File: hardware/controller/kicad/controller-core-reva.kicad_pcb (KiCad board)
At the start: 2 copper layers, 141.6 x 135.2 mm, 138 parts, among them J101 12V_ISOLATED_INPUT / JST XH, J102 STM_SWD / 1x6 2.54mm, J103 ESP_UART / 1x6 2.54mm, J104 UI_LINK / IDC 2x8 2.54mm, J105 JP13 NTC / 2 vías, J106 JP5 FLOW ADAPTER / VCC-GND-OC, J107 JP14 DOOR / contacto seco, J108 JP16 VISUAL V1..V8 / XH-8, J109 JP22 WATER / RED-WHITE-BLACK, J110 USB-C SERVICE / USB 2.0, J111 USB BENCH POWER / OPEN, J112 24V_ACTUATOR_INPUT / JST XH, J113 JP3 VALVE / JST XH, J114 POWER MONITOR / MEASURE ONLY, J115 JP8 GRINDER / 320VDC, J117 JP24 PUMP / 230VAC, J118 JP17 MAINS / L-N, Q501 SI2308A, U101 STM32G431RBT6, U201 ESP32-S3-WROOM-1-N8R8, U203 USBLC6-2SC6, U301 AP63203WU-7, U302 TPS22918DBVR, U501 DRV8876PWPR, U502 UCC27517DBVR, U601 TPS3828-33DBVR, U602 SN74LVC2G08DCTR

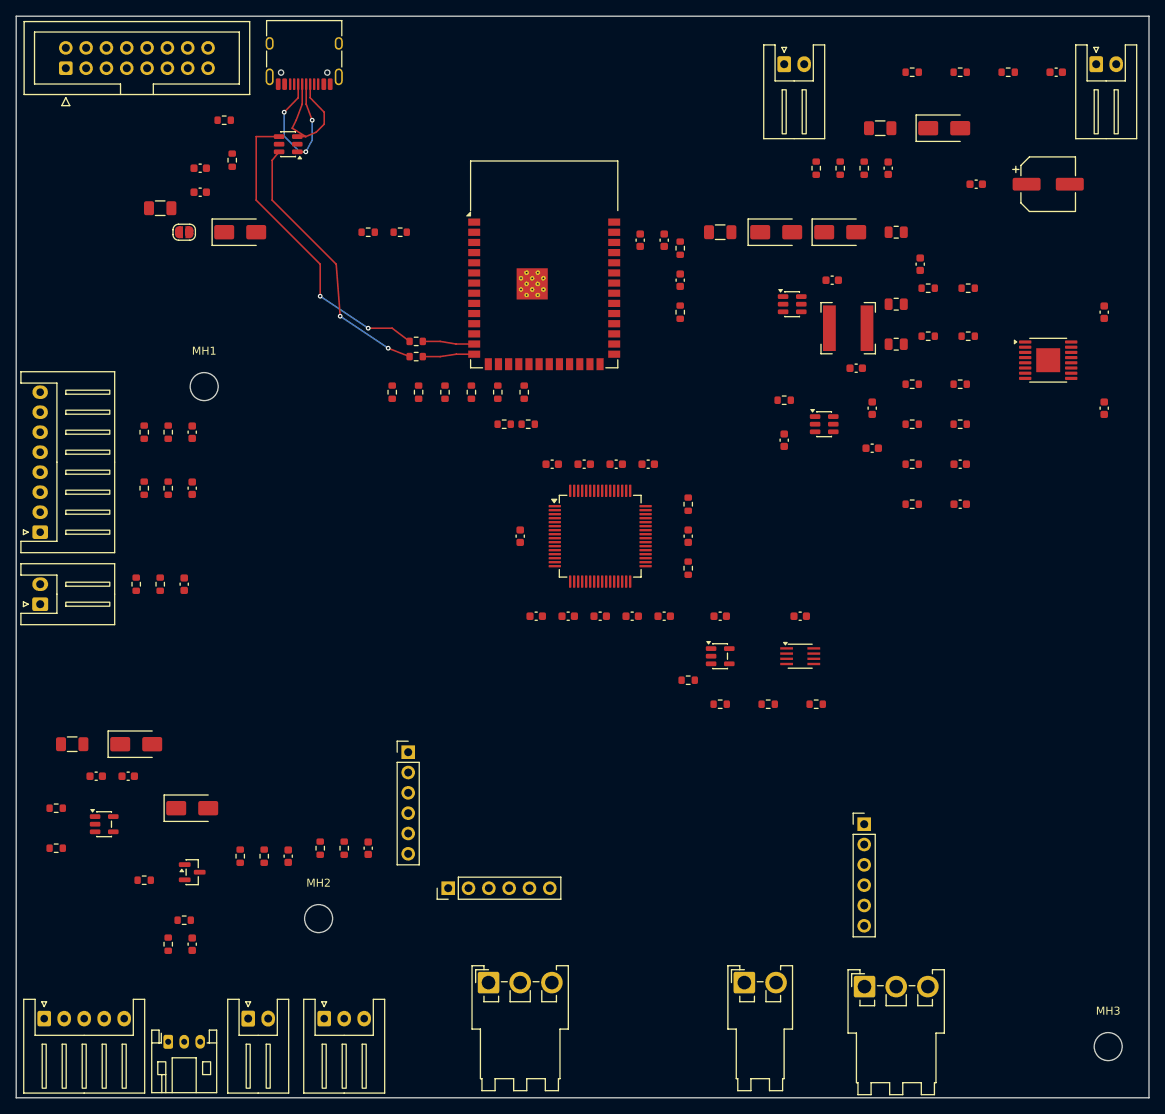
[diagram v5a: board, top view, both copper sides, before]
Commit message: Integrate onboard mains supply into controller PCB
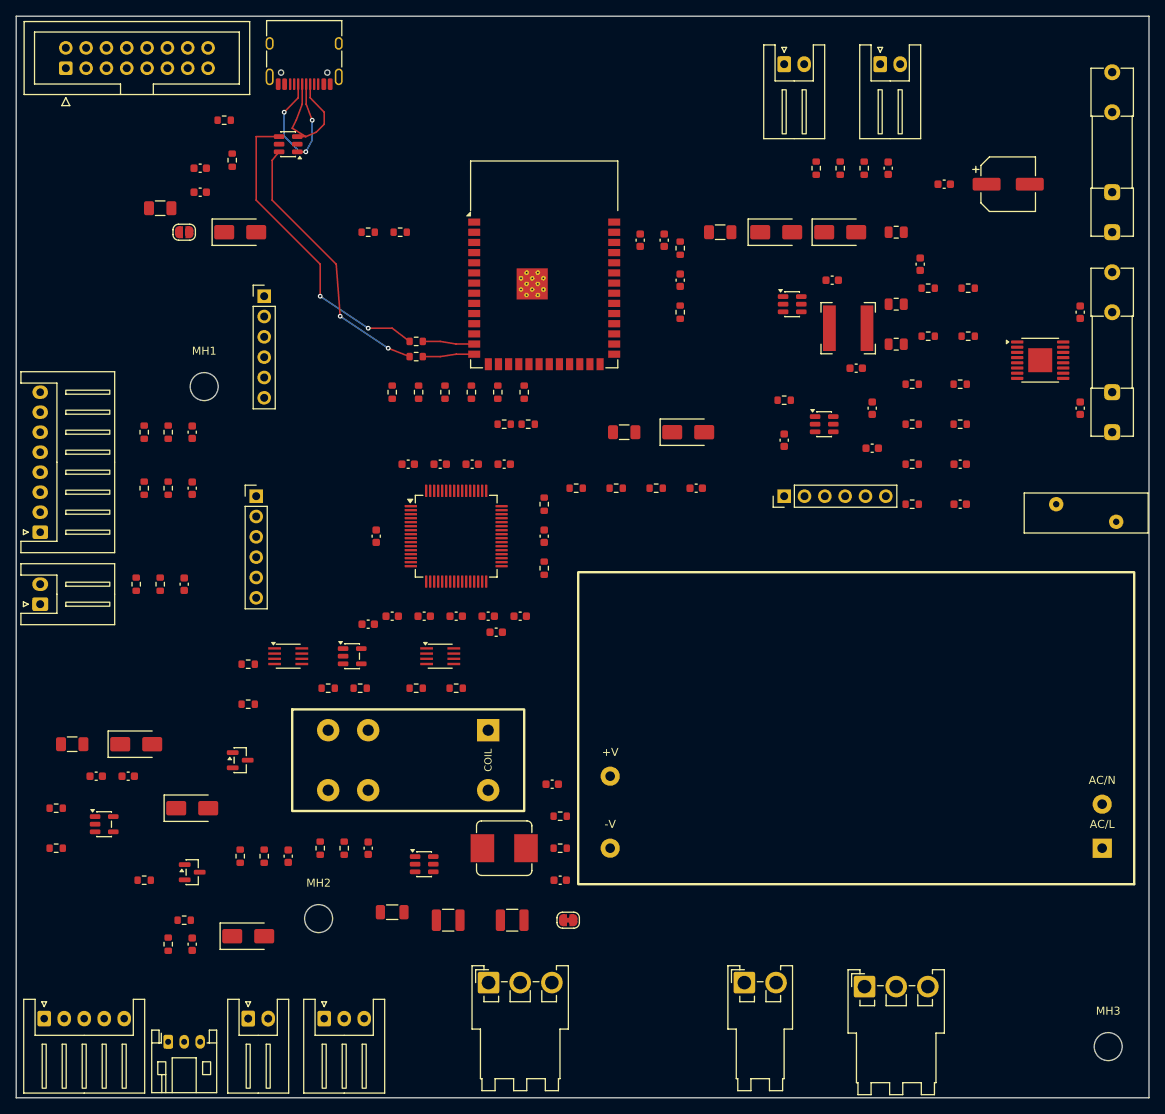
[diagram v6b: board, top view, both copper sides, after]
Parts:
- added C310: 10uF / 50V input, Capacitor_SMD:C_1206_3216Metric, F.Cu at (47.0, 112.0)
- added C311: 22uF / 25V output A, Capacitor_SMD:C_1210_3225Metric, F.Cu at (54.0, 113.0)
- added C312: 22uF / 25V output B, Capacitor_SMD:C_1210_3225Metric, F.Cu at (62.0, 113.0)
- added C313: 100nF / BST, Capacitor_SMD:C_0603_1608Metric, F.Cu at (67.0, 96.0)
- added C314: 56pF / feed-forward, Capacitor_SMD:C_0603_1608Metric, F.Cu at (68.0, 108.0)
- added D701: SS34 / relay flyback, Diode_SMD:D_SMA, F.Cu at (29.0, 115.0)
- added F701: T10A / 250V MAIN / provisional, Fuse:Fuseholder_Clip-5x20mm_Littelfuse_111_Inline_P20.00x5.00mm_D1.05mm_Horizontal, F.Cu at (137.0, 52.0)
- added F702: T1A / PSU / provisional, Fuse:Fuseholder_Clip-5x20mm_Littelfuse_111_Inline_P20.00x5.00mm_D1.05mm_Horizontal, F.Cu at (137.0, 27.0)
- added J121: 24V INTERNAL SELECT / OPEN FOR BENCH, Jumper:SolderJumper-2_P1.3mm_Bridged_RoundedPad1.0x1.5mm, F.Cu at (69.0, 113.0)
- added K701: G5RL-1A-E-TV8 DC24, OpenSaeco:Relay_SPST_Omron_G5RL-1A-E-TV8, F.Cu at (49.0, 93.0)
- added L302: 10uH / 3.5A, Inductor_SMD:L_Bourns_SRP7028A_7.3x6.6mm, F.Cu at (61.0, 104.0)
- added PS701: IRM-30-24, OpenSaeco:MeanWell_IRM-30_THT, F.Cu at (105.0, 89.0)
- added Q701: SI2308A / relay coil, Package_TO_SOT_SMD:SOT-23, F.Cu at (28.0, 93.0)
- added R302: 249k / 12V FB high, Resistor_SMD:R_0603_1608Metric, F.Cu at (68.0, 100.0)
- added R303: 18k / 12V FB low, Resistor_SMD:R_0603_1608Metric, F.Cu at (68.0, 104.0)
- added R801: 33 / relay gate, Resistor_SMD:R_0603_1608Metric, F.Cu at (29.0, 81.0)
- added R802: 100k / relay off, Resistor_SMD:R_0603_1608Metric, F.Cu at (29.0, 86.0)
- added RV701: 275VAC MOV / energy TBD, Varistor:RV_Disc_D15.5mm_W5mm_P7.5mm, F.Cu at (130.0, 61.0)
- added U303: AP63200WU-7 / 24V to 12V, Package_TO_SOT_SMD:TSOT-23-6, F.Cu at (51.0, 106.0)
- added U603: SN74LVC2G08DCTR, Package_SO:SSOP-8_2.95x2.8mm_P0.65mm, F.Cu at (34.0, 80.0)
- moved C702 68.8 mm to (85.0, 59.0)
- moved R706 68.1 mm to (80.0, 59.0)
- moved R705 67.5 mm to (75.0, 59.0)
- moved R704 66.8 mm to (70.0, 59.0)
- moved J102 59.8 mm to (31.0, 35.0)
- moved J103 54.6 mm to (30.0, 60.0), turned to 0 degrees
- moved D304 49.7 mm to (84.0, 52.0)
- moved F303 49.7 mm to (76.0, 52.0)
- moved U601 46.0 mm to (42.0, 80.0)
- moved R602 45.0 mm to (43.0, 84.0)
- moved R604 45.0 mm to (55.0, 84.0)
- moved R601 45.0 mm to (39.0, 84.0)
- moved U602 45.0 mm to (53.0, 80.0)
- moved R603 44.0 mm to (50.0, 84.0)
- moved C601 44.0 mm to (44.0, 76.0)
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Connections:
- J118 pad 1: /MAINS_L_SWITCHED -> /MAINS_L_IN
- U101 pad 60: unconnected-(U101-PB7-Pad60) -> /MAINS_ARM_RAW
